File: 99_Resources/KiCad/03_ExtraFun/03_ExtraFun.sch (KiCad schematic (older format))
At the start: 14 parts

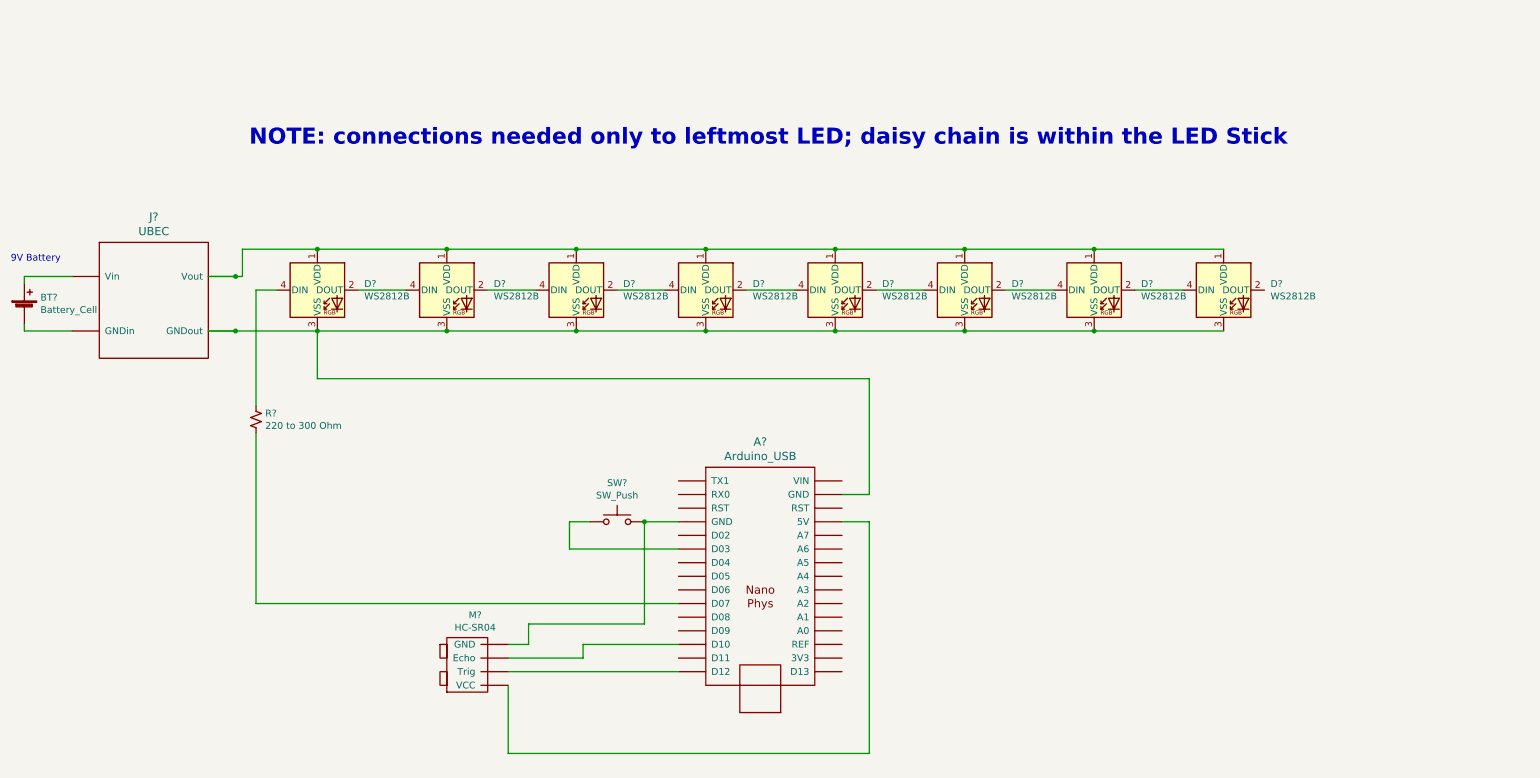
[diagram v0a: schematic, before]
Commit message: update schematic 03_SonarRangeDetector_ExtraFun
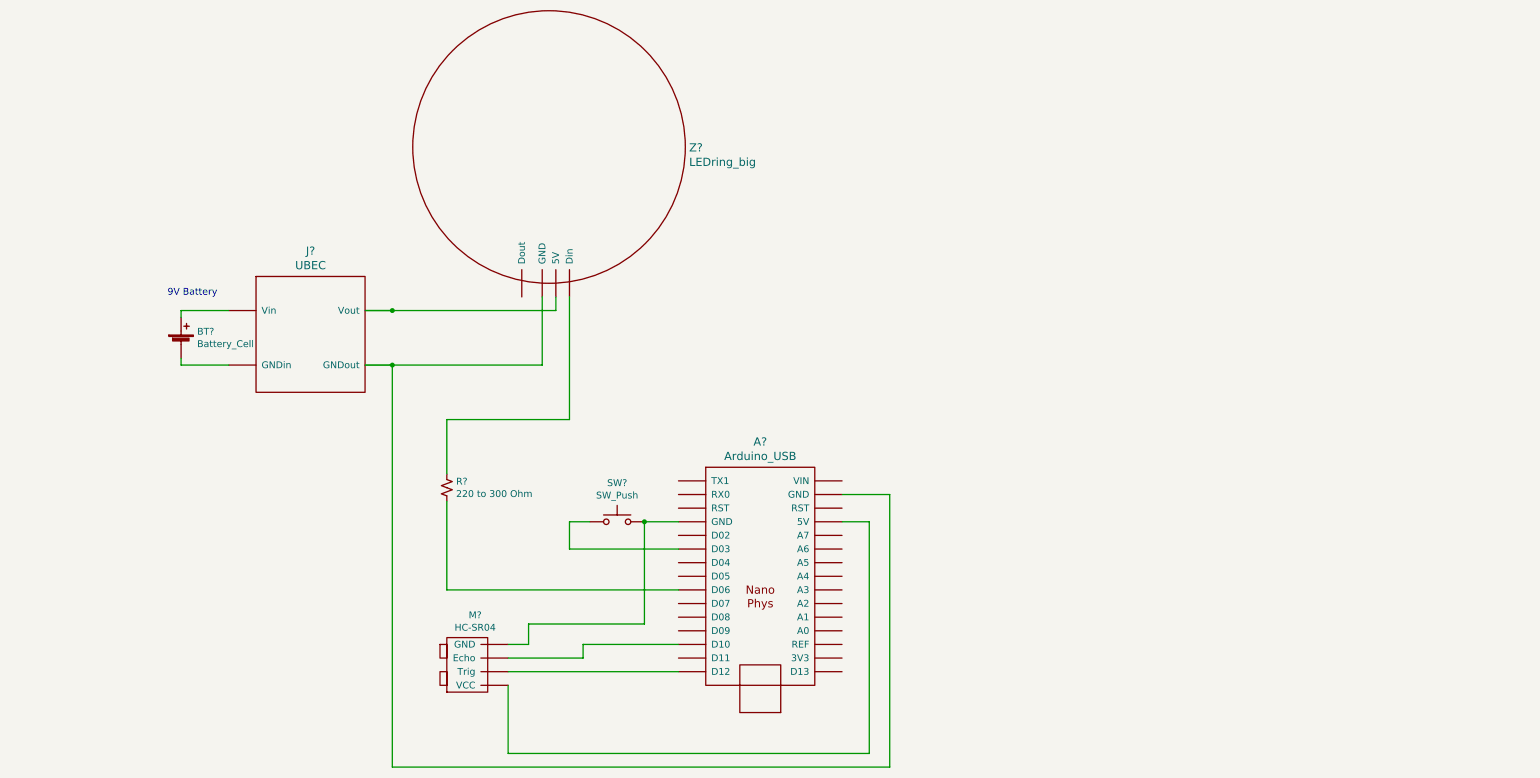
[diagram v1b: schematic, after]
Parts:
- removed D? (x8): WS2812B, LED_SMD:LED_WS2812B_PLCC4_5.0x5.0mm_P3.2mm, symbol LED:WS2812B
- added Z?: LEDring_big, symbol mdoLibrary:LEDring_big
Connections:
- wire segments 55 -> 35
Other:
- note removed: "NOTE: connections needed only to leftmost LED; daisy chain is within the LED Stick"
- moved on the sheet: BT?, R?
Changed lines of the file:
@@
 Sheet 1 1
 Title "03 Sonar Range Detector - Extra Fun"
-Date "2023-04-18"
+Date "2023-04-22"
 Rev ""
 Comp "Author: https://github.com/Mark-MDO47/ArduinoClass/tree/master"
@@
 L Device:R_Small_US R?
 U 1 1 64387B62
-P 2550 4100
-F 0 "R?" H 2618 4146 50  0000 L CNN
-F 1 "220 to 300 Ohm" H 2618 4055 50  0000 L CNN
-F 2 "" H 2550 4100 50  0001 C CNN
-F 3 "~" H 2550 4100 50  0001 C CNN
-	1    2550 4100
+P 3950 4600
+F 0 "R?" H 4018 4646 50  0000 L CNN
+F 1 "220 to 300 Ohm" H 4018 4555 50  0000 L CNN
+F 2 "" H 3950 4600 50  0001 C CNN
+F 3 "~" H 3950 4600 50  0001 C CNN
+	1    3950 4600
 	1    0    0    -1
 $EndComp
@@
 Wire Wire Line
 	4850 4850 4850 5050
-$Comp
-L LED:WS2812B D?
-U 1 1 6439D7A1
-P 3000 3150
-F 0 "D?" H 3344 3196 50  0000 L CNN
-F 1 "WS2812B" H 3344 3105 50  0000 L CNN
-F 2 "LED_SMD:LED_WS2812B_PLCC4_5.0x5.0mm_P3.2mm" H 3050 2850 50  0001 L TNN
-F 3 "https://cdn-shop.adafruit.com/datasheets/WS2812B.pdf" H 3100 2775 50  0001 L TNN
-	1    3000 3150
-	1    0    0    -1
-$EndComp
-$Comp
-L LED:WS2812B D?
-U 1 1 6439F025
-P 3950 3150
-F 0 "D?" H 4294 3196 50  0000 L CNN
-F 1 "WS2812B" H 4294 3105 50  0000 L CNN
-F 2 "LED_SMD:LED_WS2812B_PLCC4_5.0x5.0mm_P3.2mm" H 4000 2850 50  0001 L TNN
-F 3 "https://cdn-shop.adafruit.com/datasheets/WS2812B.pdf" H 4050 2775 50  0001 L TNN
-	1    3950 3150
-	1    0    0    -1
-$EndComp
-$Comp
-L LED:WS2812B D?
-U 1 1 643A1A23
-P 4900 3150
-F 0 "D?" H 5244 3196 50  0000 L CNN
-F 1 "WS2812B" H 5244 3105 50  0000 L CNN
-F 2 "LED_SMD:LED_WS2812B_PLCC4_5.0x5.0mm_P3.2mm" H 4950 2850 50  0001 L TNN
-F 3 "https://cdn-shop.adafruit.com/datasheets/WS2812B.pdf" H 5000 2775 50  0001 L TNN
-	1    4900 3150
-	1    0    0    -1
-$EndComp
-$Comp
-L LED:WS2812B D?
-U 1 1 643A1E95
-P 5850 3150
-F 0 "D?" H 6194 3196 50  0000 L CNN
-F 1 "WS2812B" H 6194 3105 50  0000 L CNN
-F 2 "LED_SMD:LED_WS2812B_PLCC4_5.0x5.0mm_P3.2mm" H 5900 2850 50  0001 L TNN
-F 3 "https://cdn-shop.adafruit.com/datasheets/WS2812B.pdf" H 5950 2775 50  0001 L TNN
-	1    5850 3150
-	1    0    0    -1
-$EndComp
-$Comp
-L LED:WS2812B D?
-U 1 1 643A29C1
-P 6800 3150
-F 0 "D?" H 7144 3196 50  0000 L CNN
-F 1 "WS2812B" H 7144 3105 50  0000 L CNN
-F 2 "LED_SMD:LED_WS2812B_PLCC4_5.0x5.0mm_P3.2mm" H 6850 2850 50  0001 L TNN
-F 3 "https://cdn-shop.adafruit.com/datasheets/WS2812B.pdf" H 6900 2775 50  0001 L TNN
-	1    6800 3150
-	1    0    0    -1
-$EndComp
-$Comp
-L LED:WS2812B D?
-U 1 1 643A2BA5
-P 7750 3150
-F 0 "D?" H 8094 3196 50  0000 L CNN
-F 1 "WS2812B" H 8094 3105 50  0000 L CNN
-F 2 "LED_SMD:LED_WS2812B_PLCC4_5.0x5.0mm_P3.2mm" H 7800 2850 50  0001 L TNN
-F 3 "https://cdn-shop.adafruit.com/datasheets/WS2812B.pdf" H 7850 2775 50  0001 L TNN
-	1    7750 3150
-	1    0    0    -1
-$EndComp
-$Comp
-L LED:WS2812B D?
-U 1 1 643A2DB0
-P 8700 3150
-F 0 "D?" H 9044 3196 50  0000 L CNN
-F 1 "WS2812B" H 9044 3105 50  0000 L CNN
-F 2 "LED_SMD:LED_WS2812B_PLCC4_5.0x5.0mm_P3.2mm" H 8750 2850 50  0001 L TNN
-F 3 "https://cdn-shop.adafruit.com/datasheets/WS2812B.pdf" H 8800 2775 50  0001 L TNN
-	1    8700 3150
-	1    0    0    -1
-$EndComp
-$Comp
-L LED:WS2812B D?
-U 1 1 643A2FD8
-P 9650 3150
-F 0 "D?" H 9994 3196 50  0000 L CNN
-F 1 "WS2812B" H 9994 3105 50  0000 L CNN
-F 2 "LED_SMD:LED_WS2812B_PLCC4_5.0x5.0mm_P3.2mm" H 9700 2850 50  0001 L TNN
-F 3 "https://cdn-shop.adafruit.com/datasheets/WS2812B.pdf" H 9750 2775 50  0001 L TNN
-	1    9650 3150
-	1    0    0    -1
-$EndComp
-Wire Wire Line
-	2700 3150 2550 3150
-Wire Wire Line
-	3300 3150 3650 3150
-Wire Wire Line
-	4250 3150 4600 3150
-Wire Wire Line
-	5200 3150 5550 3150
-Wire Wire Line
-	6150 3150 6500 3150
-Wire Wire Line
-	7100 3150 7450 3150
-Wire Wire Line
-	8050 3150 8400 3150
-Wire Wire Line
-	9000 3150 9350 3150
 Wire Wire Line
 	5650 4850 5400 4850
-Wire Wire Line
-	9650 3450 8700 3450
-Wire Wire Line
-	8700 3450 7750 3450
-Connection ~ 8700 3450
-Wire Wire Line
-	7750 3450 6800 3450
-Connection ~ 7750 3450
-Wire Wire Line
-	6800 3450 5850 3450
-Connection ~ 6800 3450
-Wire Wire Line
-	5850 3450 4900 3450
-Connection ~ 5850 3450
-Wire Wire Line
-	4900 3450 3950 3450
-Connection ~ 4900 3450
-Wire Wire Line
-	3950 3450 3000 3450
-Connection ~ 3950 3450
-Connection ~ 3000 3450
-Wire Wire Line
-	7050 3800 3000 3800
-Wire Wire Line
-	3000 3450 3000 3800
-Wire Wire Line
-	9650 2850 8700 2850
-Wire Wire Line
-	8700 2850 7750 2850
-Connection ~ 8700 2850
-Wire Wire Line
-	7750 2850 6800 2850
-Connection ~ 7750 2850
-Wire Wire Line
-	6800 2850 5850 2850
-Connection ~ 6800 2850
-Wire Wire Line
-	5850 2850 4900 2850
-Connection ~ 5850 2850
-Wire Wire Line
-	4900 2850 3950 2850
-Connection ~ 4900 2850
-Wire Wire Line
-	3950 2850 3000 2850
-Connection ~ 3950 2850
-Text Notes 2500 2100 0    118  ~ 24
-NOTE: connections needed only to leftmost LED; daisy chain is within the LED Stick
-Wire Wire Line
-	5650 5450 2550 5450
-Wire Wire Line
-	6850 4650 7050 4650
-Wire Wire Line
-	7050 4650 7050 3800
 Wire Wire Line
 	6850 4850 7050 4850
@@
 L mdoLibrary:UBEC J?
 U 1 1 6440393A
-P 1700 3300
-F 0 "J?" H 1800 3987 60  0000 C CNN
-F 1 "UBEC" H 1800 3881 60  0000 C CNN
-F 2 "" H 1700 3300 60  0001 C CNN
-F 3 "" H 1700 3300 60  0001 C CNN
-	1    1700 3300
+P 2850 3550
+F 0 "J?" H 2950 4237 60  0000 C CNN
+F 1 "UBEC" H 2950 4131 60  0000 C CNN
+F 2 "" H 2850 3550 60  0001 C CNN
+F 3 "" H 2850 3550 60  0001 C CNN
+	1    2850 3550
 	1    0    0    -1
 $EndComp
 Wire Wire Line
-	2550 4200 2550 5450
+	3350 3700 3550 3700
 Wire Wire Line
-	2550 4000 2550 3150
-Wire Wire Line
-	2200 3450 2400 3450
-Wire Wire Line
-	2450 2850 3000 2850
-Wire Wire Line
-	2200 3050 2400 3050
-Connection ~ 3000 2850
-Wire Wire Line
-	2400 3050 2450 3050
-Wire Wire Line
-	2450 3050 2450 2850
-Connection ~ 2400 3050
-Wire Wire Line
-	2400 3450 3000 3450
-Connection ~ 2400 3450
+	3350 3300 3550 3300
 $Comp
 L Device:Battery_Cell BT?
 U 1 1 6440ACA4
-P 850 3300
-F 0 "BT?" H 968 3396 50  0000 L CNN
-F 1 "Battery_Cell" H 968 3305 50  0000 L CNN
-F 2 "" V 850 3360 50  0001 C CNN
-F 3 "~" V 850 3360 50  0001 C CNN
-	1    850  3300
+P 2000 3550
+F 0 "BT?" H 2118 3646 50  0000 L CNN
+F 1 "Battery_Cell" H 2118 3555 50  0000 L CNN
+F 2 "" V 2000 3610 50  0001 C CNN
+F 3 "~" V 2000 3610 50  0001 C CNN
+	1    2000 3550
 	1    0    0    -1
 $EndComp
 Wire Wire Line
-	1200 3450 850  3450
+	2350 3700 2000 3700
 Wire Wire Line
-	850  3450 850  3400
+	2000 3700 2000 3650
 Wire Wire Line
-	850  3100 850  3050
+	2000 3350 2000 3300
 Wire Wire Line
-	850  3050 1200 3050
-Text Notes 750  2950 0    50   ~ 0
+	2000 3300 2350 3300
+Text Notes 1900 3200 0    50   ~ 0
 9V Battery
+$Comp
+L mdoLibrary:LEDring_big Z?
+U 1 1 64448FEE
+P 4700 2100
+F 0 "Z?" H 5728 2095 60  0000 L CNN
+F 1 "LEDring_big" H 5728 1989 60  0000 L CNN
+F 2 "" H 4700 2250 60  0001 C CNN
+F 3 "" H 4700 2250 60  0001 C CNN
+	1    4700 2100
+	1    0    0    -1
+$EndComp
+Wire Wire Line
+	4750 3200 4750 3300
+Wire Wire Line
+	3550 3300 4750 3300
+Connection ~ 3550 3300
+Wire Wire Line
+	3550 3700 4650 3700
+Wire Wire Line
+	4650 3700 4650 3200
+Connection ~ 3550 3700
+Wire Wire Line
+	3950 4700 3950 5350
+Wire Wire Line
+	3950 4100 4850 4100
+Wire Wire Line
+	3950 4100 3950 4500
+Wire Wire Line
+	4850 3200 4850 4100
+Wire Wire Line
+	3950 5350 5650 5350
+Wire Wire Line
+	7200 4650 7200 6650
+Wire Wire Line
+	7200 6650 3550 6650
+Wire Wire Line
+	3550 6650 3550 3700
+Wire Wire Line
+	6850 4650 7200 4650
 $EndSCHEMATC
